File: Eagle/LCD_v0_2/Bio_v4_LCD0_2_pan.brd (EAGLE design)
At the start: 69.3 x 82.2 mm, 78 parts, among them X1 MINI-USB, X2 16MHz, X3 FH12-08S-1SH, X4 MINI-USB, X5 16MHz, X6 FH12-08S-1SH

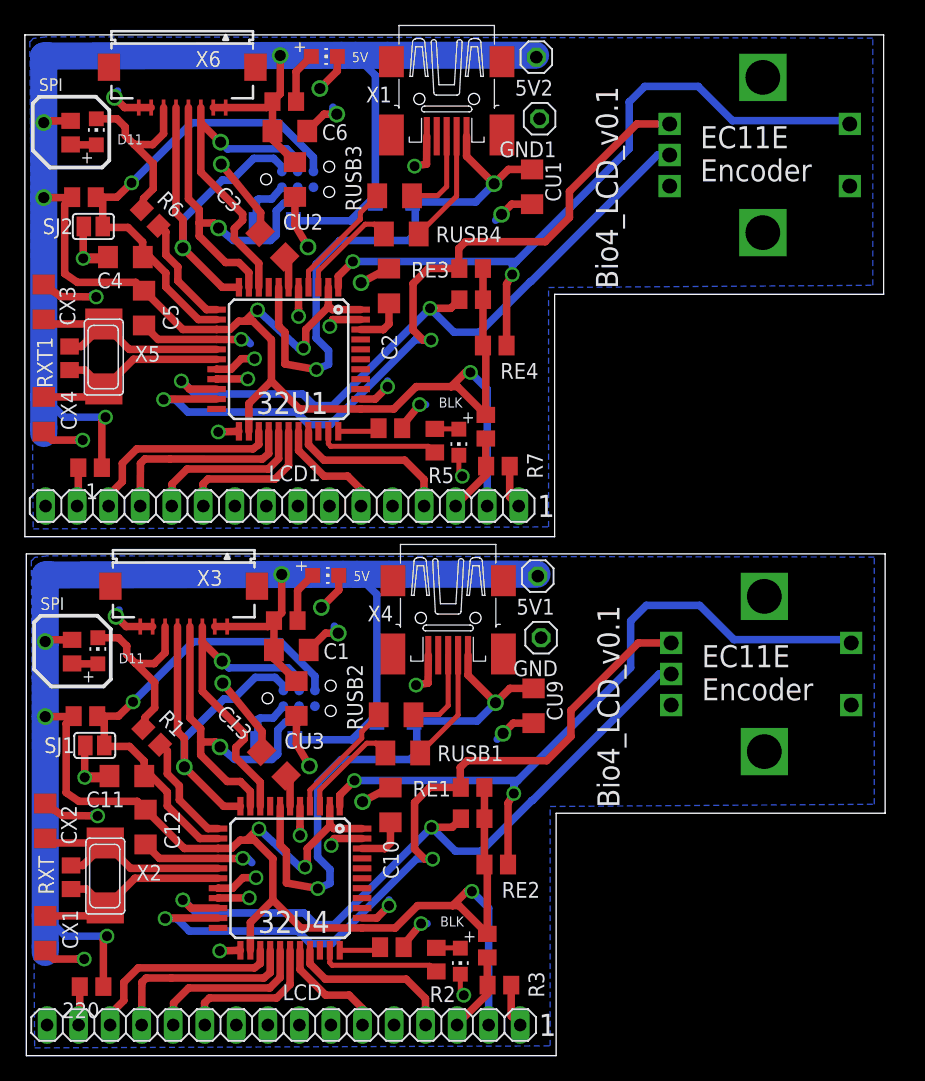
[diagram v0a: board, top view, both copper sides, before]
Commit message: swapped flex connector on LCD SPI, changed D11 pin by the SS/RXLED pin instead, removed SPI pull-up + diode
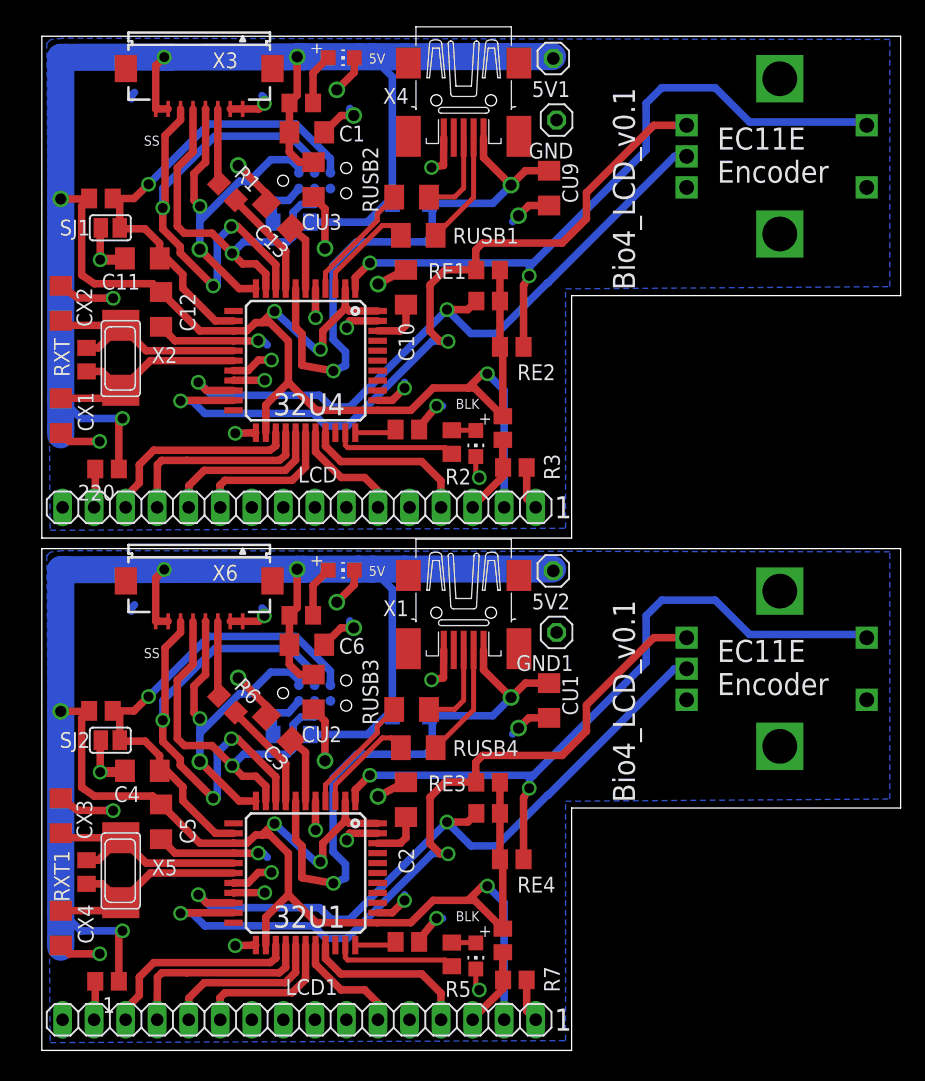
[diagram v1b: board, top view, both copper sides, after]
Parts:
- removed LDSLAVE, LDSLAVE1: RED, adafruit:CHIP-LED0805
- removed RK18: 10k, rcl:R0805
- removed RK9: 10k, resistor:M0805
- 32U1, 32U4: value ATMEGA32U4 -> 32U4
- RK8: device rcl:R0805 -> resistor:M0805
- moved RK5 73.8 mm to (37.2, 9.22)
- moved R1 44.3 mm to (15.0, 69.5)
- moved C13 44.1 mm to (19.2, 67.6)
- moved CU3 41.8 mm to (22.0, 70.5)
- moved C11 41.7 mm to (8.17, 64.1)
- moved CON_ISP 41.7 mm to (19.5, 70.4)
- moved D2 41.7 mm to (20.2, 67.1)
- moved D4 41.7 mm to (29.8, 68.6)
- moved GND 41.7 mm to (41.5, 75.3)
- moved R13 41.7 mm to (21.0, 76.7)
- moved R3 41.7 mm to (38.2, 47.3)
- moved RE1 41.7 mm to (36.0, 63.2)
- moved RK7 41.7 mm to (29.5, 50.4)
- moved RUSB1 41.7 mm to (30.4, 66.0)
- moved X2 41.7 mm to (6.43, 56.1)
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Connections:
- removed net N$22: LDSLAVE.A, RK18.2
- removed net N$9 (its old number): LCD1.3, R7.1, RK8.2
- net +5V/1: now also X3.7, X3.8; no longer RK18.1, X3.1, X3.2
- net +5V/2: now also RK8.2, X6.7, X6.8; no longer RK8.1, RK9.2, X6.1, X6.2
- net CS_32U1: now also X6.3; no longer LDSLAVE1.C, X6.6
- net CS_32U4: now also X3.3; no longer LDSLAVE.C, X3.6
- net D11*: no longer R1.2
- net D11*1: no longer R6.2
- net D7*1: now also RK8.1; no longer RK9.1
- net GND: now also X3.1, X3.2; no longer X3.7, X3.8
- net GND1: now also X6.1, X6.2; no longer X6.7, X6.8
- net MISO: now also X3.4; no longer X3.5
- net MISO1: now also X6.4; no longer X6.5
- net MOSI: now also X3.5; no longer X3.4
- net MOSI1: now also X6.5; no longer X6.4
- net N$8: now also LCD1.3, R7.1; no longer LDSLAVE1.A
- net RXLED: now also R1.2
- net RXLED1: now also R6.2
- net SCK: now also X3.6; no longer X3.3
- net SCK1: now also X6.6; no longer X6.3
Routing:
- net SCK: track 26.9 -> 46.2 mm, vias 1 -> 3
- net SCK1: track 26.9 -> 46.2 mm, vias 1 -> 3
- net CS_32U4: track 15.3 -> 6.05 mm
- net CS_32U1: track 15.3 -> 6.05 mm
- net D11*: track 9.19 -> 0.00 mm
- net D11*1: track 9.19 -> 0.00 mm
- net RXLED1: track 0.00 -> 8.79 mm
- net RXLED: track 0.00 -> 8.79 mm
- net N$9 (its old number): track 6.47 -> 0.00 mm
- net N$8: track 2.08 -> 6.47 mm
- net N$1: track 2.55 -> 5.42 mm
- net N$7: track 2.55 -> 5.42 mm
- net N$22: track 2.08 -> 0.00 mm
- net GND: track 72.8 -> 70.7 mm
- net GND1: track 72.8 -> 70.7 mm
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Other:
- board size 69.3 x 82.2 mm -> 69.2 x 81.7 mm
- board text added: "SS"
- board text added: "Screen v0.1"
- board text removed: "220"
- board text removed: "32U1"
- board text removed: "32U4"
- board text removed: "5V1"
- board text removed: "5V2"
- board text removed: "C1"
- board text removed: "C10"
- board text removed: "C11"
- board text removed: "C12"
- board text removed: "C13"
- board text removed: "C2"
- board text removed: "C3"
- board text removed: "C4"
- board text removed: "C5"
- board text removed: "C6"
- board text removed: "CON_ISP"
- board text removed: "CON_ISP1"
- board text removed: "CU1"
- board text removed: "CU2"
- board text removed: "CU3"
- board text removed: "CU9"
- board text removed: "CX1"
- board text removed: "CX2"
- board text removed: "CX3"
- board text removed: "CX4"
- board text removed: "D1"
- board text removed: "D11"
- board text removed: "D2"
- board text removed: "D3"
- board text removed: "D4"
- board text removed: "GND"
- board text removed: "GND1"
- board text removed: "LCD"
- board text removed: "LCD1"
- board text removed: "PID"
- board text removed: "R1"
- board text removed: "R2"
- board text removed: "R3"
- board text removed: "R5"
- board text removed: "R6"
- board text removed: "R7"
- board text removed: "RE1"
- board text removed: "RE2"
- board text removed: "RE3"
- board text removed: "RE4"
- board text removed: "RUSB1"
- board text removed: "RUSB2"
- board text removed: "RUSB3"
- board text removed: "RUSB4"
- board text removed: "RXT"
- board text removed: "RXT1"
- board text removed: "SJ1"
- board text removed: "SJ2"
- board text removed: "SPI"
- board text removed: "Screen"
- board text removed: "X1"
- board text removed: "X2"
- board text removed: "X3"
- board text removed: "X4"
- board text removed: "X5"
- board text removed: "X6"
